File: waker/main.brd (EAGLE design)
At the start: 100 x 80 mm, 51 parts, among them IC1 C8051F381-GM, IC3 N25Q512A, IC6 MPU-9250, P0.0 PTR1TP10R, SW2 PTR1TP10R, U1 MCP73831, U2 TPS61200

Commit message: Modified circuit
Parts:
- added R16: 10k, reg,cap:1005
- added R17: 100, reg,cap:1005
- R15: value 100k -> 10k
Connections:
- new net N$11: D2.A, R13.P$2, R16.P$2, S1.3, S1.4
- new net N$12: IC1.32
- new net PWM: IC1.12, R15.P$2, R17.P$2
- net N$5: now also R16.P$1; no longer D2.A, R13.P$2, S1.3, S1.4
- net N$8: now also R17.P$1; no longer IC1.32, R15.P$2
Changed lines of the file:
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@@
 <element name="R14" library="reg,cap" package="1005" value="10k" x="2.54" y="-179.07"/>
 <element name="FET1" library="MOSFET" package="SOT23" value="DMN3404L" x="2.54" y="-185.42"/>
-<element name="R15" library="reg,cap" package="1005" value="100k" x="2.54" y="-191.77"/>
+<element name="R15" library="reg,cap" package="1005" value="10k" x="2.54" y="-191.77"/>
 <element name="R1" library="SparkFun-Resistors" package="0603-RES" value="" x="3.81" y="-195.58">
 <attribute name="PROD_ID" value="RES-08296" x="3.81" y="-195.58" size="1.778" layer="27" display="off"/>
@@
 <attribute name="TP_SIGNAL_NAME" value="" x="2.54" y="-203.2" size="1.778" layer="27" display="off"/>
 </element>
+<element name="R16" library="reg,cap" package="1005" value="10k" x="2.54" y="-207.01"/>
+<element name="R17" library="reg,cap" package="1005" value="100" x="2.54" y="-212.09"/>
 </elements>
 <signals>
@@
 </signal>
 <signal name="N$5">
-<contactref element="S1" pad="3"/>
-<contactref element="S1" pad="4"/>
-<contactref element="R13" pad="P$2"/>
-<contactref element="D2" pad="A"/>
 <contactref element="IC1" pad="1"/>
-<wire x1="1.76" y1="-168.11" x2="3.14" y2="-173.99" width="0" layer="19" extent="1-1"/>
-<wire x1="5.86" y1="-168.11" x2="1.76" y2="-168.11" width="0" layer="19" extent="1-1"/>
-<wire x1="6.53" y1="-160.02" x2="5.86" y2="-168.11" width="0" layer="19" extent="1-1"/>
-<wire x1="3.625" y1="-131.6" x2="6.53" y2="-160.02" width="0" layer="19" extent="1-1"/>
+<contactref element="R16" pad="P$1"/>
+<wire x1="3.625" y1="-131.6" x2="1.94" y2="-207.01" width="0" layer="19" extent="1-1"/>
 </signal>
 <signal name="N$6">
@@
 <wire x1="3.625" y1="-132.1" x2="6.53" y2="-165.1" width="0" layer="19" extent="1-1"/>
 </signal>
-<signal name="N$8">
-<contactref element="FET1" pad="G"/>
+<signal name="PWM">
 <contactref element="R15" pad="P$2"/>
-<contactref element="IC1" pad="32"/>
-<wire x1="1.59" y1="-186.62" x2="3.14" y2="-191.77" width="0" layer="19" extent="1-1"/>
-<wire x1="4.6" y1="-130.625" x2="1.59" y2="-186.62" width="0" layer="19" extent="1-1"/>
+<contactref element="IC1" pad="12"/>
+<contactref element="R17" pad="P$2"/>
+<wire x1="3.14" y1="-191.77" x2="3.14" y2="-212.09" width="0" layer="19" extent="1-1"/>
+<wire x1="6.1" y1="-136.075" x2="3.14" y2="-191.77" width="0" layer="19" extent="1-1"/>
 </signal>
 <signal name="N$10">
@@
 <wire x1="2.54" y1="-184.22" x2="2.54" y2="-199.39" width="0" layer="19" extent="1-1"/>
 </signal>
+<signal name="N$11">
+<contactref element="S1" pad="3"/>
+<contactref element="S1" pad="4"/>
+<contactref element="R13" pad="P$2"/>
+<contactref element="D2" pad="A"/>
+<contactref element="R16" pad="P$2"/>
+<wire x1="3.14" y1="-173.99" x2="3.14" y2="-207.01" width="0" layer="19" extent="1-1"/>
+<wire x1="1.76" y1="-168.11" x2="3.14" y2="-173.99" width="0" layer="19" extent="1-1"/>
+<wire x1="5.86" y1="-168.11" x2="1.76" y2="-168.11" width="0" layer="19" extent="1-1"/>
+<wire x1="6.53" y1="-160.02" x2="5.86" y2="-168.11" width="0" layer="19" extent="1-1"/>
+</signal>
+<signal name="N$12">
+<contactref element="IC1" pad="32"/>
+</signal>
+<signal name="N$8">
+<contactref element="FET1" pad="G"/>
+<contactref element="R17" pad="P$1"/>
+<wire x1="1.59" y1="-186.62" x2="1.94" y2="-212.09" width="0" layer="19" extent="1-1"/>
+</signal>
 </signals>

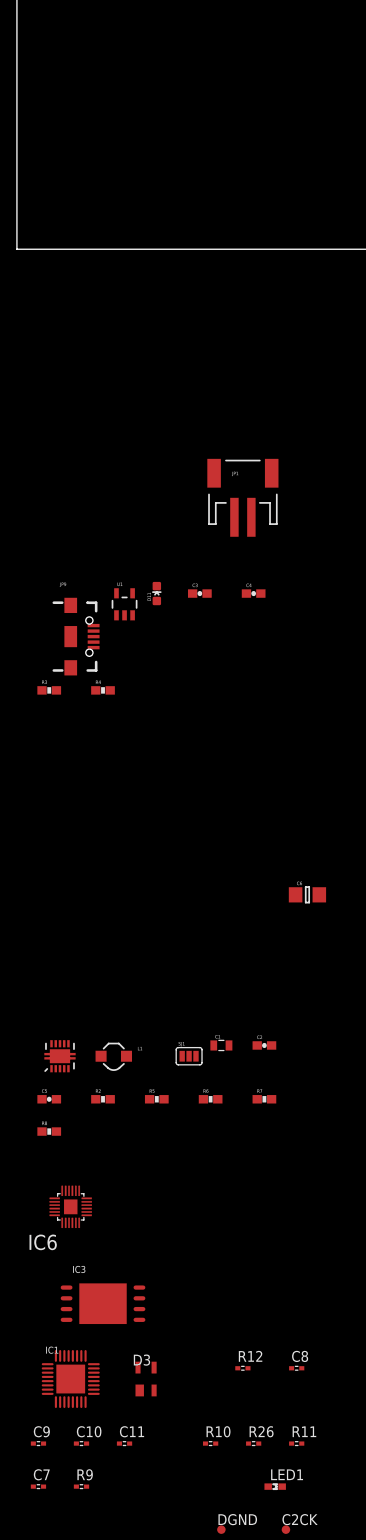
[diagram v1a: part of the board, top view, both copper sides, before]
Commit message: Put MCU, Gyro and Flash on a board
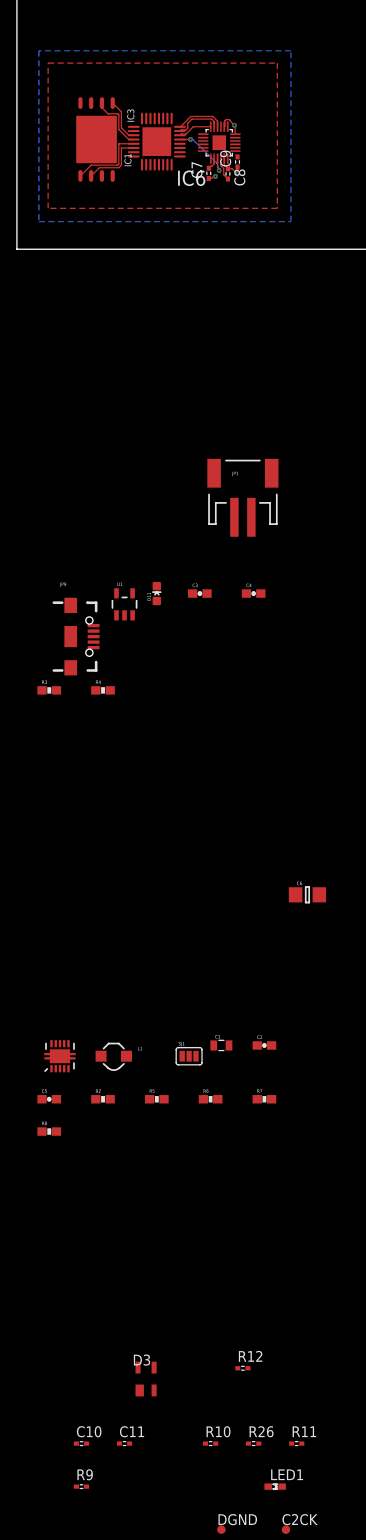
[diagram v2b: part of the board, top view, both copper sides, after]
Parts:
- moved C7 156.3 mm to (22.6, 8.95), turned to 90 degrees
- moved C9 153.1 mm to (26.0, 10.3), turned to 90 degrees
- moved IC1 146.4 mm to (16.5, 12.7), turned to 90 degrees
- moved C8 141.2 mm to (24.9, 8.89), turned to 270 degrees
- moved IC3 137.4 mm to (9.40, 13.0), turned to 270 degrees
- moved IC6 126.8 mm to (23.9, 12.6)
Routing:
- net EEPROM_MOSI: track 0.00 -> 9.26 mm
- net IMU_MISO: track 0.00 -> 7.85 mm, vias 0 -> 2
- net DGND: track 0.00 -> 7.75 mm, vias 0 -> 3
- net EEPROM_SCK: track 0.00 -> 7.57 mm
- net EEPROM_MISO: track 0.00 -> 6.86 mm
- net IMU_!CS: track 0.00 -> 5.83 mm
- net IMU_SCK: track 0.00 -> 5.70 mm
- net EEPROM_!CS: track 0.00 -> 5.17 mm
- net IMU_MOSI: track 0.00 -> 4.06 mm
- net N$13: track 0.00 -> 2.74 mm
- net VCC: track 0.00 -> 1.46 mm
- added copper zone on layer 16, net DGND
- added copper zone on layer 1, net VCC

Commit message: Puttin parts
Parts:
- removed C2CK, C2D, DGND, GND, P0.0: PTR1TP10R, testpad:TP10R
- removed C6: 10uF, CH_passive:1206
- removed R6: 1.2M, SparkFun:0603-RES
- removed R7: 220k, SparkFun:0603-RES
- removed R8: 2M, SparkFun:0603-RES
- removed SJ1: (no value), SparkFun:SJ_3_PASTE2&3
- added C12: 10uF, CH_passive:1206
- added JP2: (no value), pinhead:1X01
- added JP3: (no value), pinhead:1X03
- added R18: (no value), rcl:R0402
- C2, C5: device SparkFun:0603-CAP -> rcl:C0402K
- R1, R3, R4: device SparkFun-Resistors:0603-RES -> rcl:R0402
- R2, R5: device SparkFun:0603-RES -> rcl:R0402
- U2: value TPS61200 -> TPS61201
- moved R1 254.7 mm to (53.7, 54.2), turned to 180 degrees
- moved R14 229.0 mm to (72.6, 38.9), turned to 90 degrees
- moved R13 221.9 mm to (72.6, 36.5), turned to 270 degrees
- moved R16 215.8 mm to (15.3, 8.42)
- moved S1 213.8 mm to (72.6, 33.5)
- moved D4 213.3 mm to (70.6, 37.9), turned to 270 degrees
- moved D2 209.8 mm to (74.6, 37.9), turned to 270 degrees
- moved R10 163.0 mm to (35.5, 21.5), turned to 90 degrees
- moved D3 155.5 mm to (37.7, 20.5)
- moved R12 151.7 mm to (35.5, 19.4), turned to 90 degrees
- moved R11 151.0 mm to (19.7, 9.49), turned to 90 degrees
- moved R26 150.7 mm to (13.2, 8.95), turned to 90 degrees
- moved C10 149.8 mm to (18.3, 8.41), turned to 180 degrees
- moved C11 148.1 mm to (9.99, 7.06)
- moved R2 129.5 mm to (71.0, 14.0), turned to 270 degrees
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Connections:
- removed net 3.3V: R6.1, SJ1.1
- removed net 5V: R8.1, SJ1.3
- removed net FB: R7.2, SJ1.2, U2.10
- net C2CK: now also JP3.3; no longer C2CK.TP
- net C2D: now also JP3.2; no longer C2D.TP
- net DGND: now also JP3.1; no longer DGND.TP, GND.TP
- net GND: now also C12.2; no longer C6.2, R7.1
- net N$15: now also JP2.1; no longer P0.0.TP
- net VBAT: now also C12.1; no longer C6.1
- net VCC: now also U2.10; no longer R6.2, R8.2
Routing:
- net VBAT: track 0.00 -> 16.5 mm
- net GND: track 0.00 -> 15.3 mm, vias 0 -> 3
- net N$11: track 0.00 -> 8.48 mm
- net UVLO: track 0.00 -> 6.35 mm
- net N$6: track 0.00 -> 4.09 mm
- net VCC: track 1.46 -> 4.51 mm
- net N$2: track 0.00 -> 2.60 mm
- net N$5: track 0.00 -> 1.59 mm
- net DGND: track 7.75 -> 8.94 mm

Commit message: Modified parts places
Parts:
- removed R18: (no value), rcl:R0402
- removed SW2: PTR1TP10R, testpad:TP10R
- moved JP2 297.5 mm to (47.8, 72.6)
- moved R17 275.6 mm to (22.9, 62.7), turned to 270 degrees
- moved MP 273.4 mm to (21.1, 69.6)
- moved MN 269.9 mm to (23.8, 69.7)
- moved R15 255.5 mm to (24.7, 62.8), turned to 270 degrees
- moved FET1 252.6 mm to (23.7, 66.3)
- moved R9 222.9 mm to (50.7, 72.6), turned to 180 degrees
- moved LED1 219.9 mm to (53.5, 72.6)
- moved JP1 42.5 mm to (50.0, 7.57), turned to 90 degrees
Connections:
- removed net N$12: IC1.32
- removed net N$4: IC1.25, SW2.TP
